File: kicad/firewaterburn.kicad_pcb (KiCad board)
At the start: 2 copper layers, 20 parts, among them P201 USB_C_Plug_USB2.0, Q201 SS8050-G, Q202 SS8050-G, SW201 SW_MEC_5G, SW202 SW_MEC_5G, U201 CP2102N-A01-GQFN28, U202 ESP32-WROOM-32

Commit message: add all parts to schematic
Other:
- net class Default removed

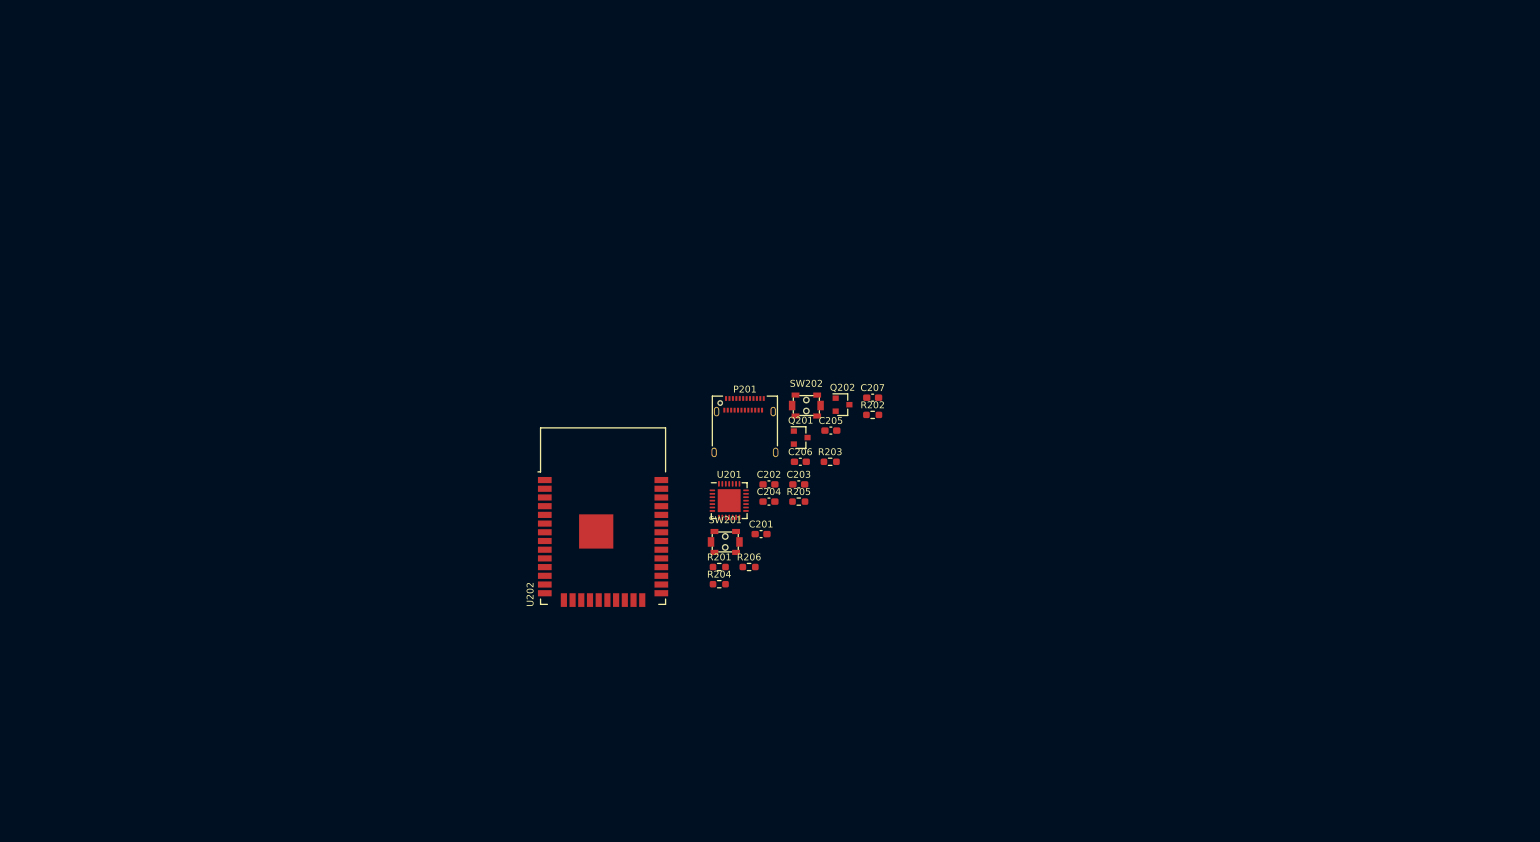
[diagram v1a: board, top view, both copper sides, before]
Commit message: refactor KiCAD Project to v6
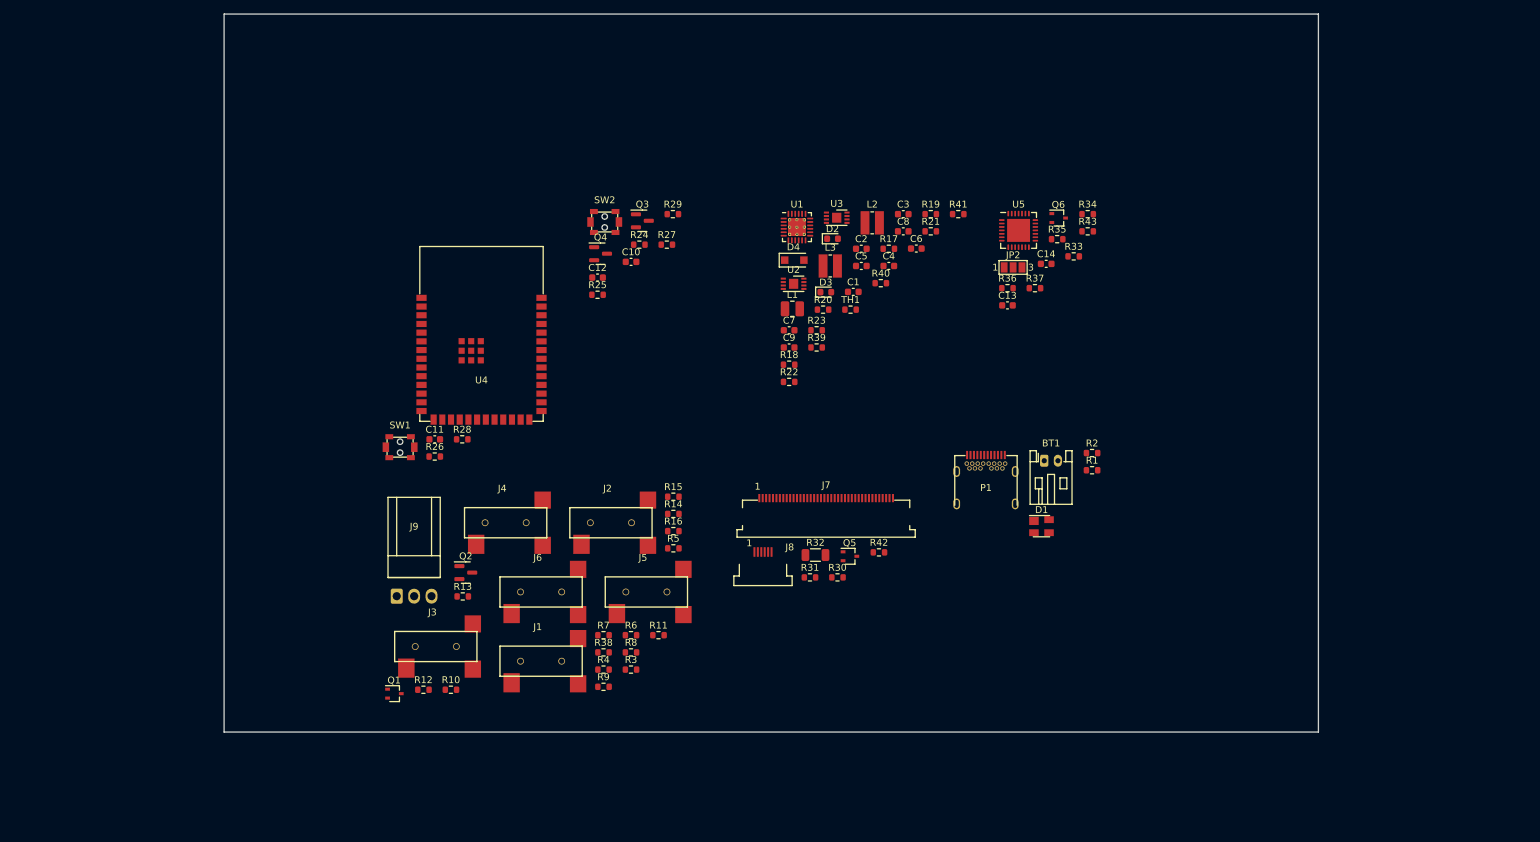
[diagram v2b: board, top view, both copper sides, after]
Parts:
- removed C201, C202, C204, C205, C207: 100n, Capacitor_SMD:C_0603_1608Metric_Pad1.08x0.95mm_HandSolder
- removed C203: 4.7µ, Capacitor_SMD:C_0603_1608Metric_Pad1.08x0.95mm_HandSolder
- removed C206: 22µ, Capacitor_SMD:C_0603_1608Metric_Pad1.08x0.95mm_HandSolder
- removed P201: USB_C_Plug_USB2.0, Connector_USB:USB_C_Receptacle_Amphenol_12401610E4-2A
- removed Q201, Q202: SS8050-G, Package_TO_SOT_SMD:SOT-23
- removed R201, R202, R206: 10k, Resistor_SMD:R_0603_1608Metric_Pad0.98x0.95mm_HandSolder
- removed R203: 22k1, Resistor_SMD:R_0603_1608Metric_Pad0.98x0.95mm_HandSolder
- removed R204: 47k5, Resistor_SMD:R_0603_1608Metric_Pad0.98x0.95mm_HandSolder
- removed R205: 2k, Resistor_SMD:R_0603_1608Metric_Pad0.98x0.95mm_HandSolder
- removed SW201, SW202: SW_MEC_5G, firewaterburn:PTS820J25MSMTRLFS
- removed U201: CP2102N-A01-GQFN28, Package_DFN_QFN:QFN-28-1EP_5x5mm_P0.5mm_EP3.35x3.35mm
- removed U202: ESP32-WROOM-32, RF_Module:ESP32-WROOM-32
- added BT1: Battery_Cell, Connector_JST:JST_PH_S2B-PH-K_1x02_P2.00mm_Horizontal, F.Cu at (181.5, 92.5)
- added C1: 1µ, Capacitor_SMD:C_0603_1608Metric, F.Cu at (153.7, 67.9)
- added C10: 100n, Capacitor_SMD:C_0603_1608Metric, F.Cu at (121.2, 63.5)
- added C11: 100n, Capacitor_SMD:C_0603_1608Metric, F.Cu at (92.6, 89.4)
- added C12: 100n, Capacitor_SMD:C_0603_1608Metric, F.Cu at (116.3, 65.8)
- added C13: 4,7µ, Capacitor_SMD:C_0603_1608Metric, F.Cu at (176.1, 69.8)
- added C14: 100n, Capacitor_SMD:C_0603_1608Metric, F.Cu at (181.8, 63.8)
- added C2: 10µ, Capacitor_SMD:C_0603_1608Metric, F.Cu at (154.8, 61.6)
- added C3: 47nF, Capacitor_SMD:C_0603_1608Metric, F.Cu at (160.9, 56.5)
- added C4: 10µ, Capacitor_SMD:C_0603_1608Metric, F.Cu at (158.8, 64.1)
- added C5: 4,7µ, Capacitor_SMD:C_0603_1608Metric, F.Cu at (154.8, 64.1)
- added C6: 10µ, Capacitor_SMD:C_0603_1608Metric, F.Cu at (162.8, 61.5)
- added C7: 4,7µ, Capacitor_SMD:C_0603_1608Metric, F.Cu at (144.3, 73.5)
- added C8: 4,7µ, Capacitor_SMD:C_0603_1608Metric, F.Cu at (160.9, 59.0)
- added C9: 10µ, Capacitor_SMD:C_0603_1608Metric, F.Cu at (144.3, 76.0)
- added D1: SP0503BAHTG, Package_TO_SOT_SMD:SOT-143, F.Cu at (181.1, 102.0)
- added D2: LED, LED_SMD:LED_0603_1608Metric, F.Cu at (150.6, 60.1)
- added D3: LED, LED_SMD:LED_0603_1608Metric, F.Cu at (149.6, 67.9)
- added D4: PMEG4010ER, Diode_SMD:D_SOD-123F, F.Cu at (145.0, 63.2)
- added J1: AudioJack2_SwitchT, z_connector:MJ-2523, F.Cu at (114.1, 121.7)
- added J2: AudioJack2_SwitchT, z_connector:MJ-2523, F.Cu at (124.3, 101.5)
- added J3: AudioJack2_SwitchT, z_connector:MJ-2523, F.Cu at (98.7, 119.6)
- added J4: AudioJack2_SwitchT, z_connector:MJ-2523, F.Cu at (108.9, 101.5)
- added J5: AudioJack2_SwitchT, z_connector:MJ-2523, F.Cu at (129.5, 111.6)
- added J6: AudioJack2_SwitchT, z_connector:MJ-2523, F.Cu at (114.1, 111.6)
- added J7: R61529 LCD, z_connector:62684-402100ALF, F.Cu at (149.7, 98.6)
- added J8: FT6236, z_connector:SFV6R-2STE1HLF, F.Cu at (140.5, 106.5)
- added J9: Conn_01x03, z_connector:Molex_KK-254_AE-6410-03A_1x03_P2.54mm_Vertical, F.Cu at (87.0, 112.3)
- added JP2: SolderJumper_3_Open, Jumper:SolderJumper-3_P1.3mm_Open_Pad1.0x1.5mm_NumberLabels, F.Cu at (177.0, 64.3)
- added L1: 1µ, Inductor_SMD:L_1008_2520Metric, F.Cu at (144.8, 70.3)
- added L2: 4µ7, Inductor_SMD:L_Wuerth_MAPI-3015, F.Cu at (156.4, 57.8)
- added L3: 4µ7, Inductor_SMD:L_Wuerth_MAPI-3015, F.Cu at (150.3, 64.1)
- added P1: USB_C_Plug_USB2.0, z_connector:USB_C_Receptacle_Amphenol_12401548E4-2A, F.Cu at (173.0, 96.5)
- added Q1: DMN61D9UWQ-13, Package_TO_SOT_SMD:SOT-323_SC-70, F.Cu at (86.7, 126.5)
- added Q2: DMP31D0U-7, Package_TO_SOT_SMD:SOT-23, F.Cu at (97.1, 108.8)
- added Q3: SS8050-G, Package_TO_SOT_SMD:SOT-23, F.Cu at (122.9, 57.5)
- added Q4: SS8050-G, Package_TO_SOT_SMD:SOT-23, F.Cu at (116.8, 62.3)
- added Q5: DMN2004WK-7, Package_TO_SOT_SMD:SOT-323_SC-70, F.Cu at (153.2, 106.4)
- added Q6: DMN2004WK-7, Package_TO_SOT_SMD:SOT-323_SC-70, F.Cu at (183.6, 57.1)
- added R1: 1k, Resistor_SMD:R_0603_1608Metric, F.Cu at (188.5, 93.9)
- added R10: 3k4, Resistor_SMD:R_0603_1608Metric, F.Cu at (95.0, 125.9)
- added R11: 4k42, Resistor_SMD:R_0603_1608Metric, F.Cu at (125.2, 118.0)
- added R12: 3k4, Resistor_SMD:R_0603_1608Metric, F.Cu at (90.9, 125.9)
- added R13: 10k, Resistor_SMD:R_0603_1608Metric, F.Cu at (96.7, 112.3)
- added R14: 4k42, Resistor_SMD:R_0603_1608Metric, F.Cu at (127.4, 100.3)
- added R15: 3k4, Resistor_SMD:R_0603_1608Metric, F.Cu at (127.4, 97.8)
- added R16: 4k42, Resistor_SMD:R_0603_1608Metric, F.Cu at (127.4, 102.8)
- added R17: 10k, Resistor_SMD:R_0603_1608Metric, F.Cu at (158.8, 61.6)
- added R18: 5k23, Resistor_SMD:R_0603_1608Metric, F.Cu at (144.3, 78.5)
- added R19: 30k1, Resistor_SMD:R_0603_1608Metric, F.Cu at (164.9, 56.5)
- added R2: 1k, Resistor_SMD:R_0603_1608Metric, F.Cu at (188.5, 91.4)
- added R20: 2k2, Resistor_SMD:R_0603_1608Metric, F.Cu at (149.2, 70.5)
- added R21: 2k2, Resistor_SMD:R_0603_1608Metric, F.Cu at (164.9, 59.0)
- added R22: 1050k, Resistor_SMD:R_0603_1608Metric, F.Cu at (144.3, 81.0)
- added R23: 120k, Resistor_SMD:R_0603_1608Metric, F.Cu at (148.3, 73.5)
- added R24: 10k, Resistor_SMD:R_0603_1608Metric, F.Cu at (122.4, 61.0)
- added R25: 10k, Resistor_SMD:R_0603_1608Metric, F.Cu at (116.3, 68.3)
- added R26: 0R, Resistor_SMD:R_0603_1608Metric, F.Cu at (92.6, 91.9)
- added R27: 0R, Resistor_SMD:R_0603_1608Metric, F.Cu at (126.5, 61.0)
- added R28: 10k, Resistor_SMD:R_0603_1608Metric, F.Cu at (96.6, 89.4)
- added R29: 0R, Resistor_SMD:R_0603_1608Metric, F.Cu at (127.3, 56.5)
- added R3: 4k42, Resistor_SMD:R_0603_1608Metric, F.Cu at (121.2, 123.0)
- added R30: 1M, Resistor_SMD:R_0603_1608Metric, F.Cu at (151.3, 109.5)
- added R31: 0R, Resistor_SMD:R_0603_1608Metric, F.Cu at (147.3, 109.5)
- added R32: 1R, Resistor_SMD:R_1206_3216Metric, F.Cu at (148.1, 106.3)
- added R33: 22k1, Resistor_SMD:R_0603_1608Metric, F.Cu at (185.8, 62.7)
- added R34: 47k5, Resistor_SMD:R_0603_1608Metric, F.Cu at (187.8, 56.5)
- added R35: 2k, Resistor_SMD:R_0603_1608Metric, F.Cu at (183.4, 60.2)
- added R36: 1M, Resistor_SMD:R_0603_1608Metric, F.Cu at (176.1, 67.3)
- added R37: 10k, Resistor_SMD:R_0603_1608Metric, F.Cu at (180.2, 67.3)
- added R38: 3k4, Resistor_SMD:R_0603_1608Metric, F.Cu at (117.2, 120.5)
- added R39: 0R, Resistor_SMD:R_0603_1608Metric, F.Cu at (148.3, 76.0)
- added R4: 3k4, Resistor_SMD:R_0603_1608Metric, F.Cu at (117.2, 123.0)
- added R40: 0R, Resistor_SMD:R_0603_1608Metric, F.Cu at (157.7, 66.6)
- added R41: 0R, Resistor_SMD:R_0603_1608Metric, F.Cu at (169.0, 56.5)
- added R42: 0R, Resistor_SMD:R_0603_1608Metric, F.Cu at (157.4, 105.9)
- added R43: 0R, Resistor_SMD:R_0603_1608Metric, F.Cu at (187.8, 59.0)
- added R5: 4k42, Resistor_SMD:R_0603_1608Metric, F.Cu at (127.4, 105.3)
- added R6: 3k4, Resistor_SMD:R_0603_1608Metric, F.Cu at (121.2, 118.0)
- added R7: 4k7, Resistor_SMD:R_0603_1608Metric, F.Cu at (117.2, 118.0)
- added R8: 4k7, Resistor_SMD:R_0603_1608Metric, F.Cu at (121.2, 120.5)
- added R9: 4k42, Resistor_SMD:R_0603_1608Metric, F.Cu at (117.2, 125.5)
- added SW1: SW_MEC_5G, z_connector:PTS820J25MSMTRLFS, F.Cu at (87.5, 90.5)
- added SW2: SW_MEC_5G, z_connector:PTS820J25MSMTRLFS, F.Cu at (117.4, 57.7)
- added TH1: NTCG163JH103JT1, Resistor_SMD:R_0603_1608Metric, F.Cu at (153.2, 70.5)
- added U1: RT9471GQW, Package_DFN_QFN:WQFN-24-1EP_4x4mm_P0.5mm_EP2.6x2.6mm_ThermalVias, F.Cu at (145.4, 58.4)
- added U2: MCP1663T-E/MNY, Package_DFN_QFN:DFN-8-1EP_3x2mm_P0.5mm_EP1.36x1.46mm, F.Cu at (144.9, 66.7)
- added U3: MCP1603-330I/MC, Package_DFN_QFN:DFN-8-1EP_3x2mm_P0.5mm_EP1.36x1.46mm, F.Cu at (151.2, 57.0)
- added U4: ESP32-S3-Rx, z_ic:ESP32-S3-WROOM-1, F.Cu at (99.4, 74.0)
- added U5: CP2102N-Axx-xQFN28, Package_DFN_QFN:QFN-28-1EP_5x5mm_P0.5mm_EP3.35x3.35mm, F.Cu at (177.8, 58.9)
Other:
- board outline added: 159.6 x 104.7 mm

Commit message: add connection to lcd
import parts into pcbnew
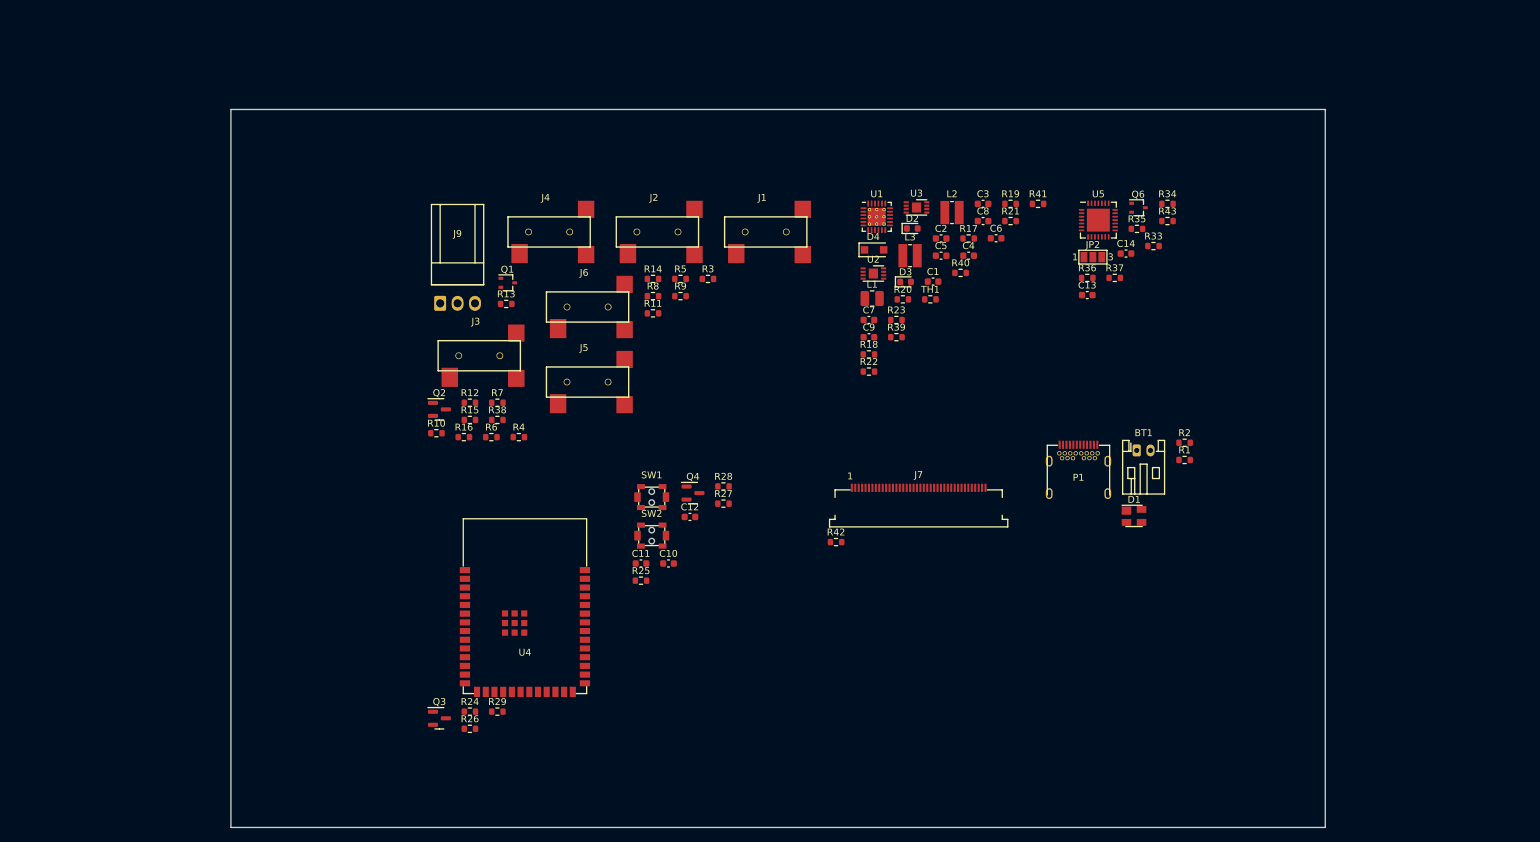
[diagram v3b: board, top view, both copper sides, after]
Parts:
- removed J8: FT6236, z_connector:SFV6R-2STE1HLF
- removed Q5: DMN2004WK-7, Package_TO_SOT_SMD:SOT-323_SC-70
- removed R30: 1M, Resistor_SMD:R_0603_1608Metric
- removed R31: 0R, Resistor_SMD:R_0603_1608Metric
- removed R32: 1R, Resistor_SMD:R_1206_3216Metric
- moved Q3 78.4 mm to (93.3, 130.1)
- moved R29 77.0 mm to (101.7, 129.1)
- moved R24 72.5 mm to (97.7, 129.1)
- moved J1 70.7 mm to (146.9, 59.1)
- moved Q1 62.2 mm to (103.2, 66.5)
- moved R9 58.1 mm to (128.4, 68.5)
- moved R3 58.1 mm to (132.4, 66.0)
- moved R8 52.1 mm to (124.4, 68.5)
- moved R11 47.0 mm to (124.4, 71.0)
- moved SW2 46.3 mm to (124.2, 103.4)
- moved C10 44.3 mm to (126.7, 107.5)
- moved J9 43.2 mm to (93.4, 69.5)
- moved R13 43.1 mm to (103.0, 69.6)
- moved J2 43.0 mm to (131.1, 59.1)
- moved J4 42.9 mm to (115.3, 59.1)
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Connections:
- J7 pad 1: unconnected-(J7-Pad1) -> Net-(J7-Pad1)
- J7 pad 10: /mcu_n_tft/RS -> unconnected-(J7-Pad10)
- J7 pad 11: /mcu_n_tft/WR -> unconnected-(J7-Pad11)
- J7 pad 12: /mcu_n_tft/RD -> unconnected-(J7-Pad12)
- J7 pad 15: /tft/TOUCH_RST -> unconnected-(J7-Pad15)
- J7 pad 16: GND -> unconnected-(J7-Pad16)
- J7 pad 17: /mcu_n_tft/DB0 -> Net-(J7-Pad1)
- J7 pad 18: /mcu_n_tft/DB1 -> Net-(J7-Pad1)
- J7 pad 19: /mcu_n_tft/DB2 -> GND
- J7 pad 2: unconnected-(J7-Pad2) -> GND
- J7 pad 20: /mcu_n_tft/DB3 -> GND
- J7 pad 21: /mcu_n_tft/DB4 -> (no net)
- J7 pad 22: /mcu_n_tft/DB5 -> (no net)
- J7 pad 23: /mcu_n_tft/DB6 -> (no net)
- J7 pad 24: /mcu_n_tft/DB7 -> (no net)
- J7 pad 25: unconnected-(J7-Pad25) -> (no net)
- J7 pad 26: unconnected-(J7-Pad26) -> (no net)
- J7 pad 27: unconnected-(J7-Pad27) -> (no net)
- J7 pad 28: unconnected-(J7-Pad28) -> (no net)
- J7 pad 29: unconnected-(J7-Pad29) -> (no net)
- J7 pad 3: unconnected-(J7-Pad3) -> /mcu_n_tft/SPICLK
- J7 pad 30: unconnected-(J7-Pad30) -> (no net)
- J7 pad 31: unconnected-(J7-Pad31) -> (no net)
- J7 pad 32: unconnected-(J7-Pad32) -> (no net)
- J7 pad 33: Net-(J7-Pad33) -> (no net)
- J7 pad 34: Net-(J7-Pad34) -> (no net)
- J7 pad 35: Net-(J7-Pad34) -> (no net)
- J7 pad 36: Net-(J7-Pad34) -> (no net)
- J7 pad 37: GND -> (no net)
- J7 pad 38: GND -> (no net)
- J7 pad 39: GND -> (no net)
- J7 pad 4: unconnected-(J7-Pad4) -> /mcu_n_tft/SPIQ
- J7 pad 40: +3V3 -> (no net)
- J7 pad 5: GND -> /mcu_n_tft/SPID
- J7 pad 6: Net-(J7-Pad33) -> /mcu_n_tft/SPICS0
- J7 pad 7: Net-(J7-Pad33) -> /mcu_n_tft/~{INT}
- J7 pad 8: unconnected-(J7-Pad8) -> /mcu_n_tft/~{PD}
- J7 pad 9: /mcu_n_tft/CS -> GND
- P1 pad A10: (no net) -> unconnected-(P1-PadA10)
- P1 pad A11: (no net) -> unconnected-(P1-PadA11)
- P1 pad A2: (no net) -> unconnected-(P1-PadA2)
- P1 pad A3: (no net) -> unconnected-(P1-PadA3)
- P1 pad B10: (no net) -> unconnected-(P1-PadB10)
- P1 pad B11: (no net) -> unconnected-(P1-PadB11)
- P1 pad B2: (no net) -> unconnected-(P1-PadB2)
- P1 pad B3: (no net) -> unconnected-(P1-PadB3)
- R1 pad 2: /mcu_n_tft/SCL -> /mcu_n_tft/SDA
- R2 pad 2: /mcu_n_tft/SDA -> /mcu_n_tft/SCL
- R42 pad 1: unconnected-(R42-Pad1) -> +3V3
- R42 pad 2: Net-(J7-Pad33) -> Net-(J7-Pad1)
- U4 pad 10: /mcu_n_tft/DB3 -> /mcu_n_tft/SPICS0
- U4 pad 11: /mcu_n_tft/DB4 -> /mcu_n_tft/SPID
- U4 pad 12: /OUTPUT/probe4 -> /OUTPUT/probe5
- U4 pad 13: /mcu_n_tft/DB5 -> /mcu_n_tft/SPIQ
- U4 pad 14: /mcu_n_tft/DB6 -> /mcu_n_tft/~{INT}
- U4 pad 16: /OUTPUT/PWM -> unconnected-(U4-Pad16)
- U4 pad 17: /OUTPUT/probe5 -> /OUTPUT/probe6
- U4 pad 18: /OUTPUT/probe6 -> /OUTPUT/TACHO
- U4 pad 19: /mcu_n_tft/CHR_INT -> /OUTPUT/PWM
- U4 pad 20: /mcu_n_tft/TCH_INT -> /mcu_n_tft/CHR_INT
- U4 pad 21: /OUTPUT/TACHO -> /mcu_n_tft/CHR_PSEL
- U4 pad 22: /mcu_n_tft/DB0 -> /USB<->UART/CHR0
- U4 pad 23: /mcu_n_tft/DB7 -> /mcu_n_tft/~{PD}
- U4 pad 24: /USB<->UART/CHR0 -> unconnected-(U4-Pad24)
- U4 pad 25: /USB<->UART/CHR1 -> unconnected-(U4-Pad25)
- U4 pad 26: /mcu_n_tft/PWM -> unconnected-(U4-Pad26)
- U4 pad 31: /tft/TOUCH_RST -> unconnected-(U4-Pad31)
- U4 pad 32: /mcu_n_tft/CS -> unconnected-(U4-Pad32)
- U4 pad 33: /mcu_n_tft/RS -> unconnected-(U4-Pad33)
- U4 pad 34: /mcu_n_tft/WR -> unconnected-(U4-Pad34)
- U4 pad 35: /mcu_n_tft/RD -> unconnected-(U4-Pad35)
- U4 pad 4: /mcu_n_tft/CHR_PSEL -> /OUTPUT/probe1
- U4 pad 5: /OUTPUT/probe1 -> /OUTPUT/probe2
- U4 pad 6: /OUTPUT/probe2 -> /OUTPUT/probe3
- U4 pad 7: /OUTPUT/probe3 -> /OUTPUT/probe4
- U4 pad 8: /mcu_n_tft/DB1 -> /USB<->UART/CHR1
- U4 pad 9: /mcu_n_tft/DB2 -> /mcu_n_tft/SPICLK
